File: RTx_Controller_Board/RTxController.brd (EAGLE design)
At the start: 161.3 x 90.2 mm, 212 parts, among them IC2 MAX5984C, J22 Debug Header, SW1 COM08720, U1 STM32F407ZXT, U3 KSZ8081, X4 MINI-USB-32005-301, X8 0826-1X1T-GJ-F

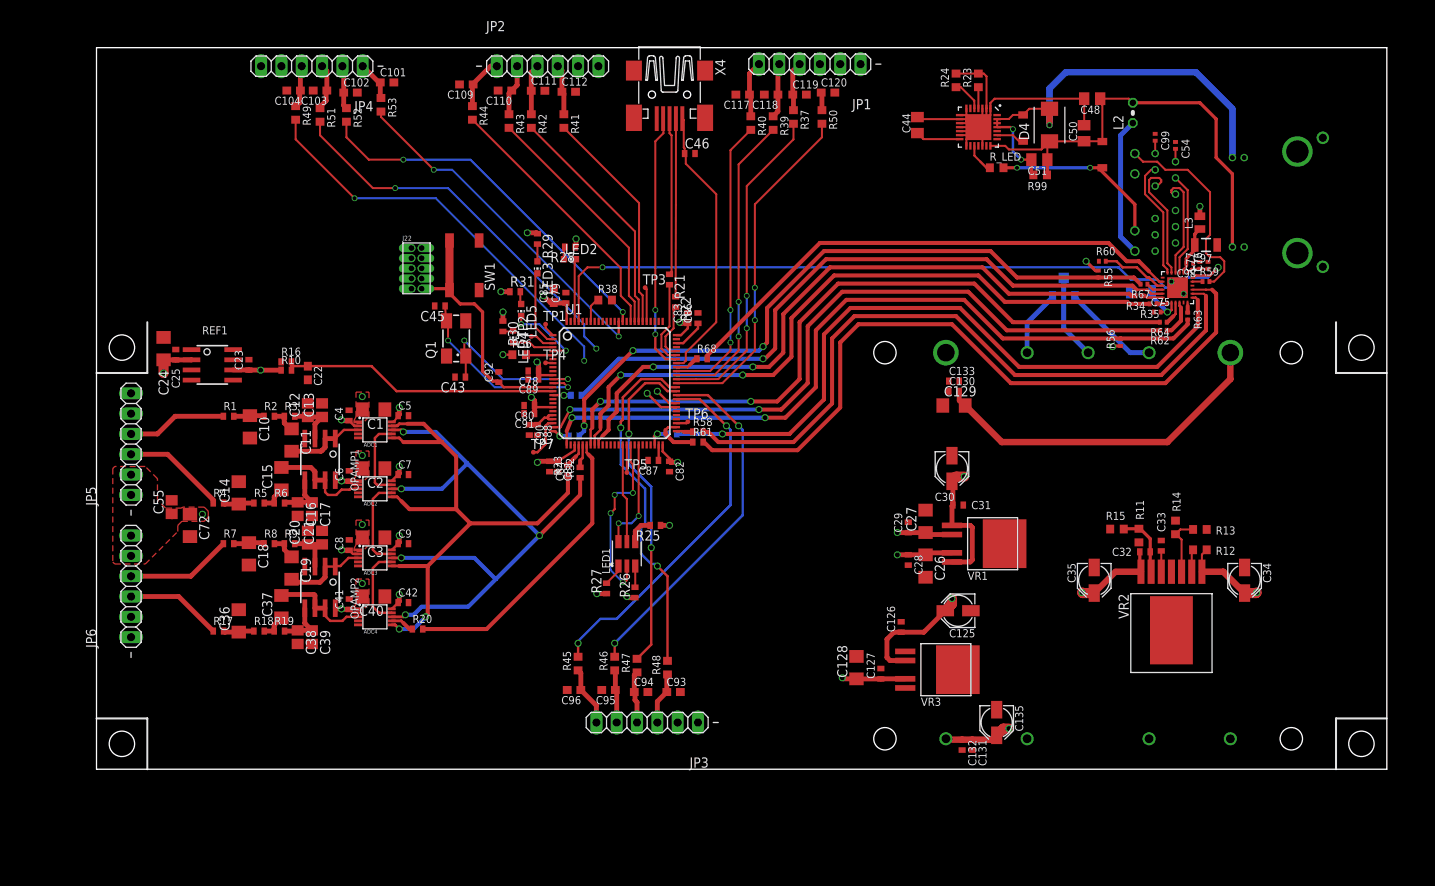
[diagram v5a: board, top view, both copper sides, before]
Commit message: Reduced board width.
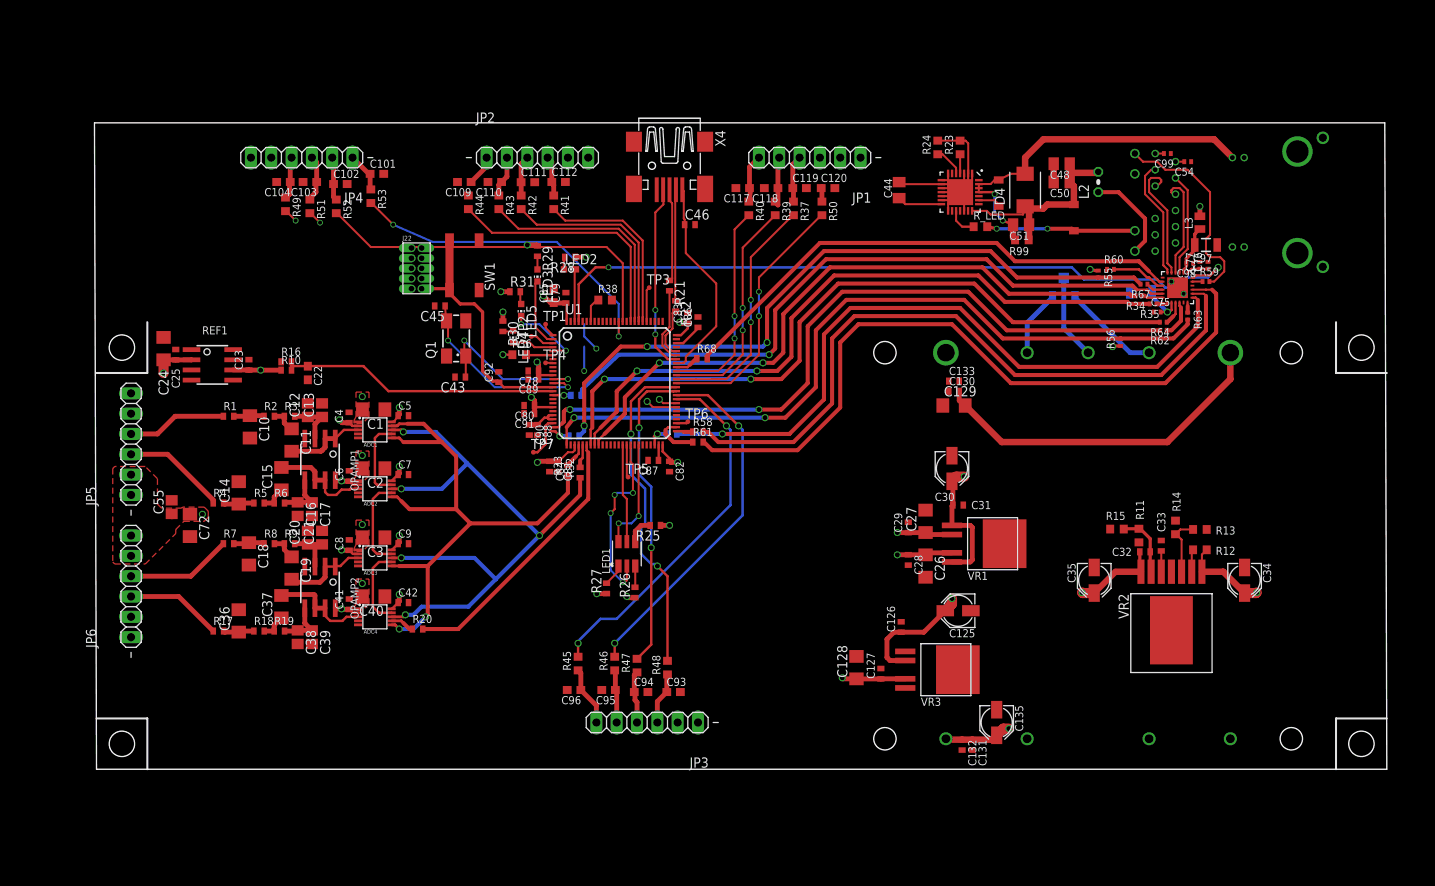
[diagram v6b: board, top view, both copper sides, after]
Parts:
- moved C109 12.2 mm to (46.0, 73.4)
- moved C120 11.9 mm to (91.4, 72.6)
- moved JP1 11.7 mm to (89.2, 76.5)
- moved C117 11.7 mm to (80.8, 72.6)
- moved C118 11.7 mm to (84.3, 72.6)
- moved C119 11.7 mm to (87.9, 72.6)
- moved C101 11.5 mm to (35.1, 74.4)
- moved JP2 11.5 mm to (55.1, 76.5)
- moved JP4 11.5 mm to (25.7, 76.5)
- moved R49 11.5 mm to (23.6, 70.6)
- moved R53 11.5 mm to (34.3, 71.6)
- moved C102 11.5 mm to (30.5, 73.2)
- moved C103 11.5 mm to (26.7, 73.4)
- moved C104 11.5 mm to (23.4, 73.4)
- moved C110 11.5 mm to (49.8, 73.4)
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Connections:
- net JTAG_TCK: now also U1.76
- net JTAG_TDI: now also U1.77
- net JTAG_TDO: now also U1.89
- net JTAG_TMS: now also U1.72
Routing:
- net WATCHDOG_LAT_OUT: track 65.0 -> 18.3 mm
- net ENABLE_LAT_OUT: track 61.9 -> 19.4 mm
- net POE+: track 56.8 -> 26.9 mm
- net POE-: track 106.1 -> 92.2 mm
- net PWM_AXIS3_U_OUT: track 41.0 -> 30.4 mm
- net PWM_AXIS3_V_OUT: track 43.3 -> 32.7 mm
- net PWM_AXIS4_U_OUT: track 36.5 -> 26.3 mm
- net PWM_AXIS4_V_OUT: track 38.4 -> 28.5 mm
- net PSE_OUTPUT: track 56.0 -> 46.2 mm, vias 3 -> 2
- net USB_ID: track 32.4 -> 23.3 mm
- net USB_VBUS: track 34.9 -> 26.0 mm
- net D+: track 22.3 -> 14.0 mm
- net D-: track 19.7 -> 11.9 mm
- net POE_LED+: track 17.4 -> 11.8 mm
- net ENABLE_AXIS3_OUT: track 28.3 -> 22.9 mm
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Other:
- board size 161.3 x 90.2 mm -> 161.5 x 80.8 mm

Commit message: PoE power supply ON/OFF connection changed to open circuit, to remain ON.
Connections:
- net GND: no longer POE.2
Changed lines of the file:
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@@
 <contactref element="C135" pad="-"/>
 <contactref element="POE" pad="4"/>
-<contactref element="POE" pad="2"/>
 <contactref element="POE" pad="3"/>
 <contactref element="C131" pad="2"/>
@@
 <wire x1="107.6706" y1="12.446" x2="101.092" y2="14.732" width="0" layer="19" extent="1-1"/>
 <wire x1="112.522" y1="7.442" x2="107.6706" y2="12.446" width="0" layer="19" extent="1-1"/>
-<wire x1="116.332" y1="3.81" x2="112.522" y2="7.442" width="0" layer="19" extent="1-1"/>
 <wire x1="109.474" y1="2.398" x2="112.522" y2="7.442" width="0" layer="19" extent="1-1"/>
 <wire x1="108.204" y1="2.398" x2="109.474" y2="2.398" width="0" layer="19" extent="1-1"/>

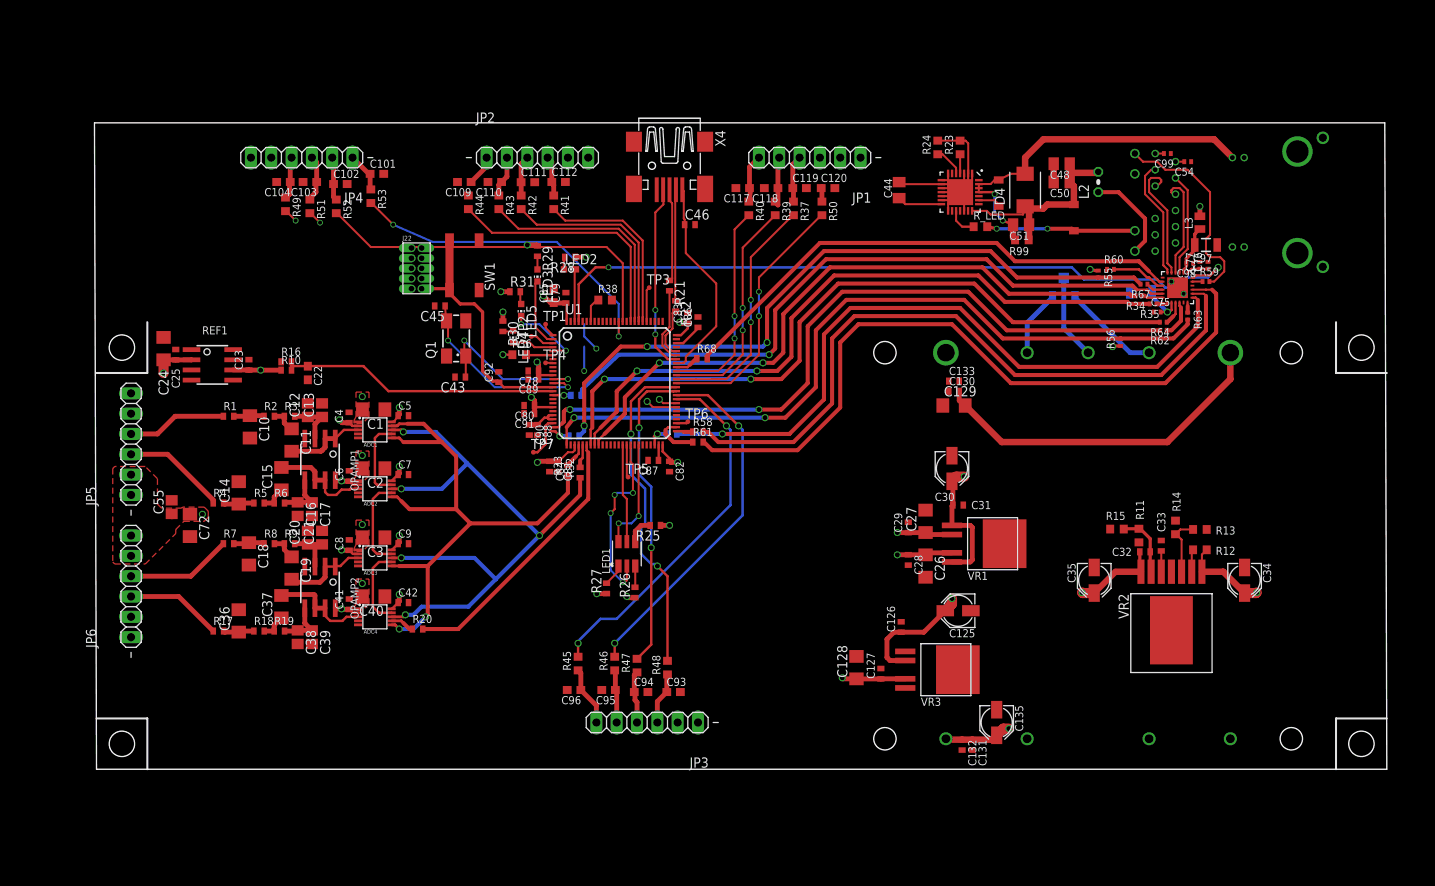
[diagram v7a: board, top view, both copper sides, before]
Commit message: Additional RTx Controller layout performed.
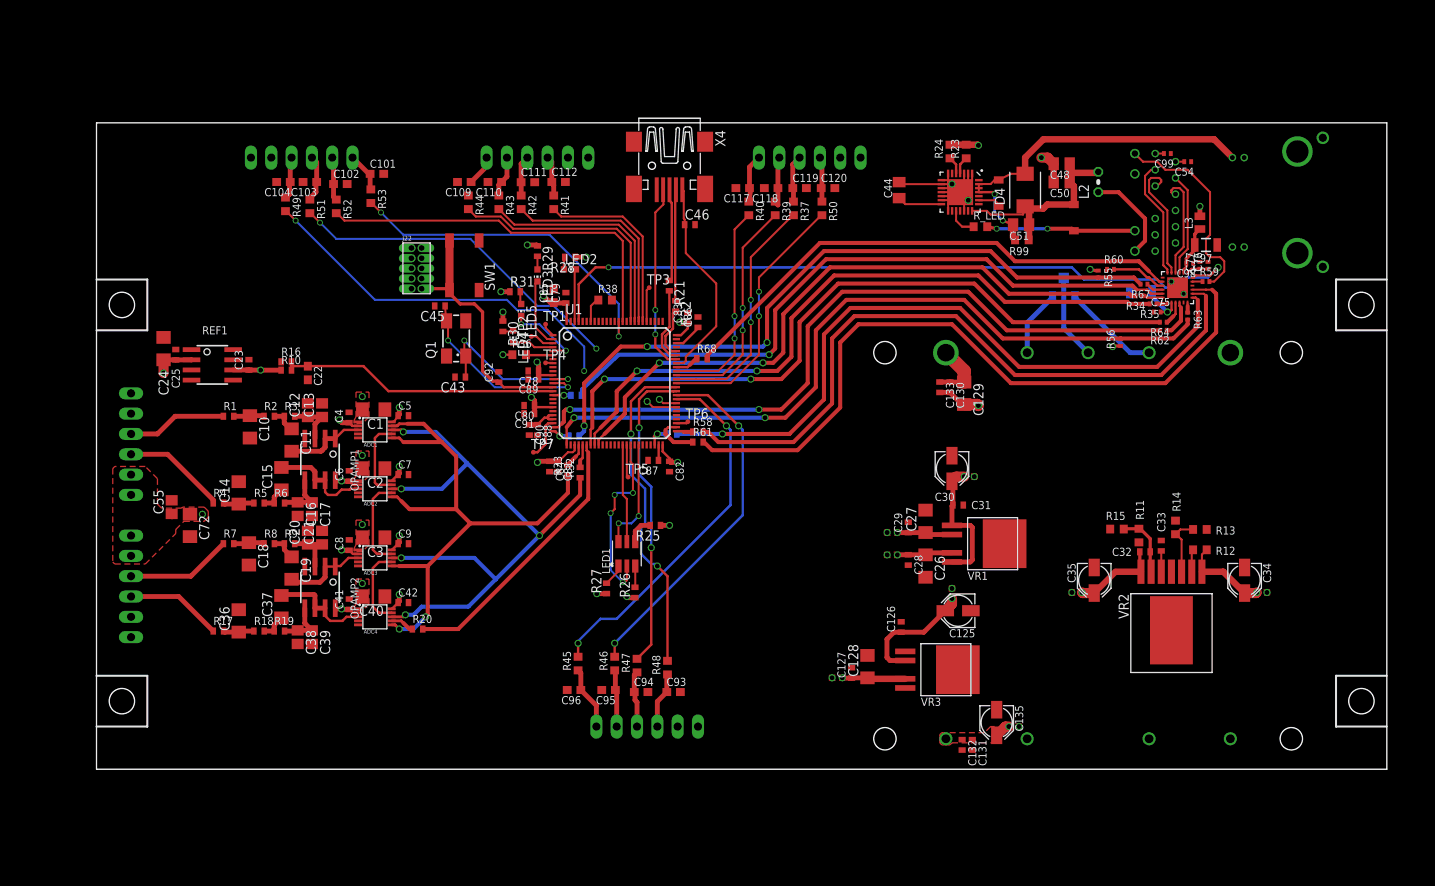
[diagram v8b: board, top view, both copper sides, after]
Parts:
- moved C127 3.66 mm to (94.4, 12.0)
- moved C129 1.98 mm to (108.5, 47.0), turned to 270 degrees
- moved C133 1.93 mm to (105.4, 47.8), turned to 270 degrees
- moved R24 1.61 mm to (106.7, 77.2)
- moved C128 1.38 mm to (96.4, 12.8)
- moved R23 0.92 mm to (108.7, 77.2)
- moved C130 0.72 mm to (106.7, 47.8), turned to 270 degrees
- moved JP3 0.51 mm to (68.8, 5.33), flipped to the bottom, turned to 0 degrees
- flipped JP1 to the bottom, turned to 0 degrees
- flipped JP2 to the bottom, turned to 180 degrees
- flipped JP4 to the bottom, turned to 0 degrees
- flipped JP5 to the bottom
- flipped JP6 to the bottom
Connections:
- net SPI_MISO: now also U1.38
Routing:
- net WATCHDOG_LAT_OUT: track 18.3 -> 60.9 mm
- net POE-: track 92.2 -> 51.4 mm, vias 0 -> 5
- net ENABLE_LAT_OUT: track 19.4 -> 56.8 mm
- net POE+: track 26.9 -> 34.6 mm
- net +9-36V: track 19.5 -> 13.0 mm, vias 2 -> 4
- net N$61: track 2.04 -> 5.79 mm
- net WATCHDOG_VERT_OUT: track 45.7 -> 47.3 mm
- net N$36: track 3.70 -> 2.21 mm
- net N$46: track 6.55 -> 7.05 mm
- net N$45: track 6.62 -> 7.13 mm
- net N$47: track 6.53 -> 7.04 mm
- net N$42: track 7.46 -> 7.97 mm
- net +8V: vias 2 -> 3
- net +5V: vias 5 -> 6
- net +3.3V: vias 23 -> 24
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- added copper zone on layer 1, net +12V
- added copper zone on layer 1, net +3.3V
- added copper zone on layer 1, net +5V
- added copper zone on layer 1, net +8V
- added copper zone on layer 1, net +9-36V
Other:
- board size 161.5 x 80.8 mm -> 161.3 x 80.8 mm
